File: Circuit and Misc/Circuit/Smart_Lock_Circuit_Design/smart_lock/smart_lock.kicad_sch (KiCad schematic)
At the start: 28 parts, among them J1 OLED, J2 RTC, J3 4x4 Keypad, J4 Ultrasonic sensor, J5 GSM, J6 Fingerprint sensor, J7 Bluetooth, Q1 IRLZ44N, Q2 BC547, SW1 Indoor button, SW2 Outdoor button, U1 24LC16, U2 LM358, U3 LM2596, U4 LM2596, U5 LM2596, U6 Bluepill_LDO, U7 STM32F103C8Tx

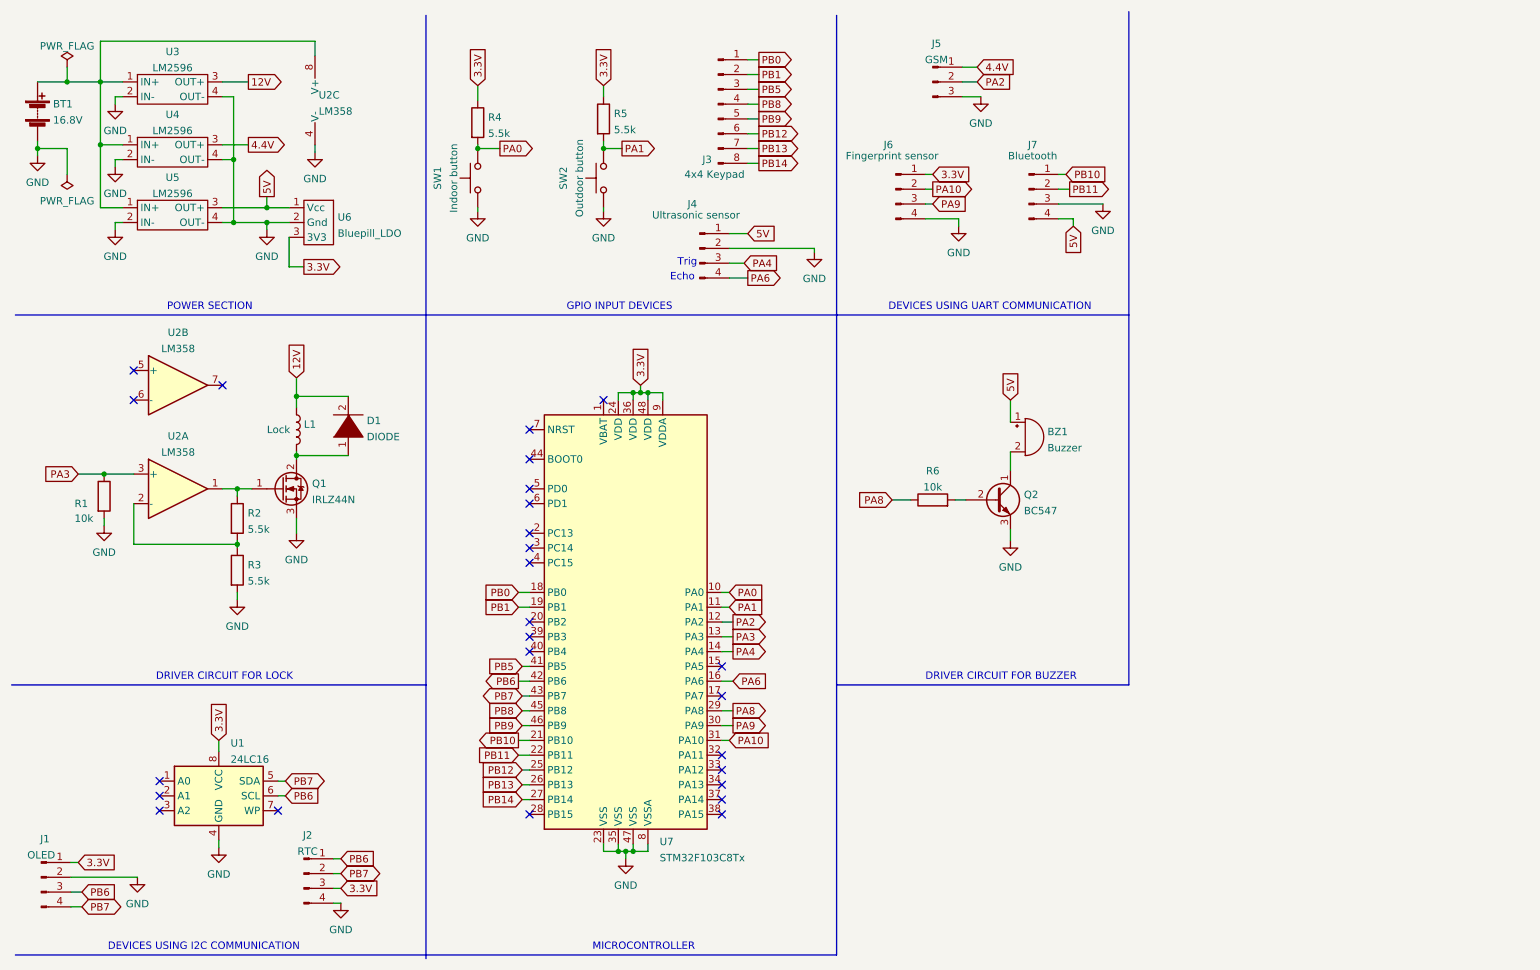
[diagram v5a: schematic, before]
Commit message: update
- Adjusted schematic (DY50 sensor is now powered using 5V)
- Added new images
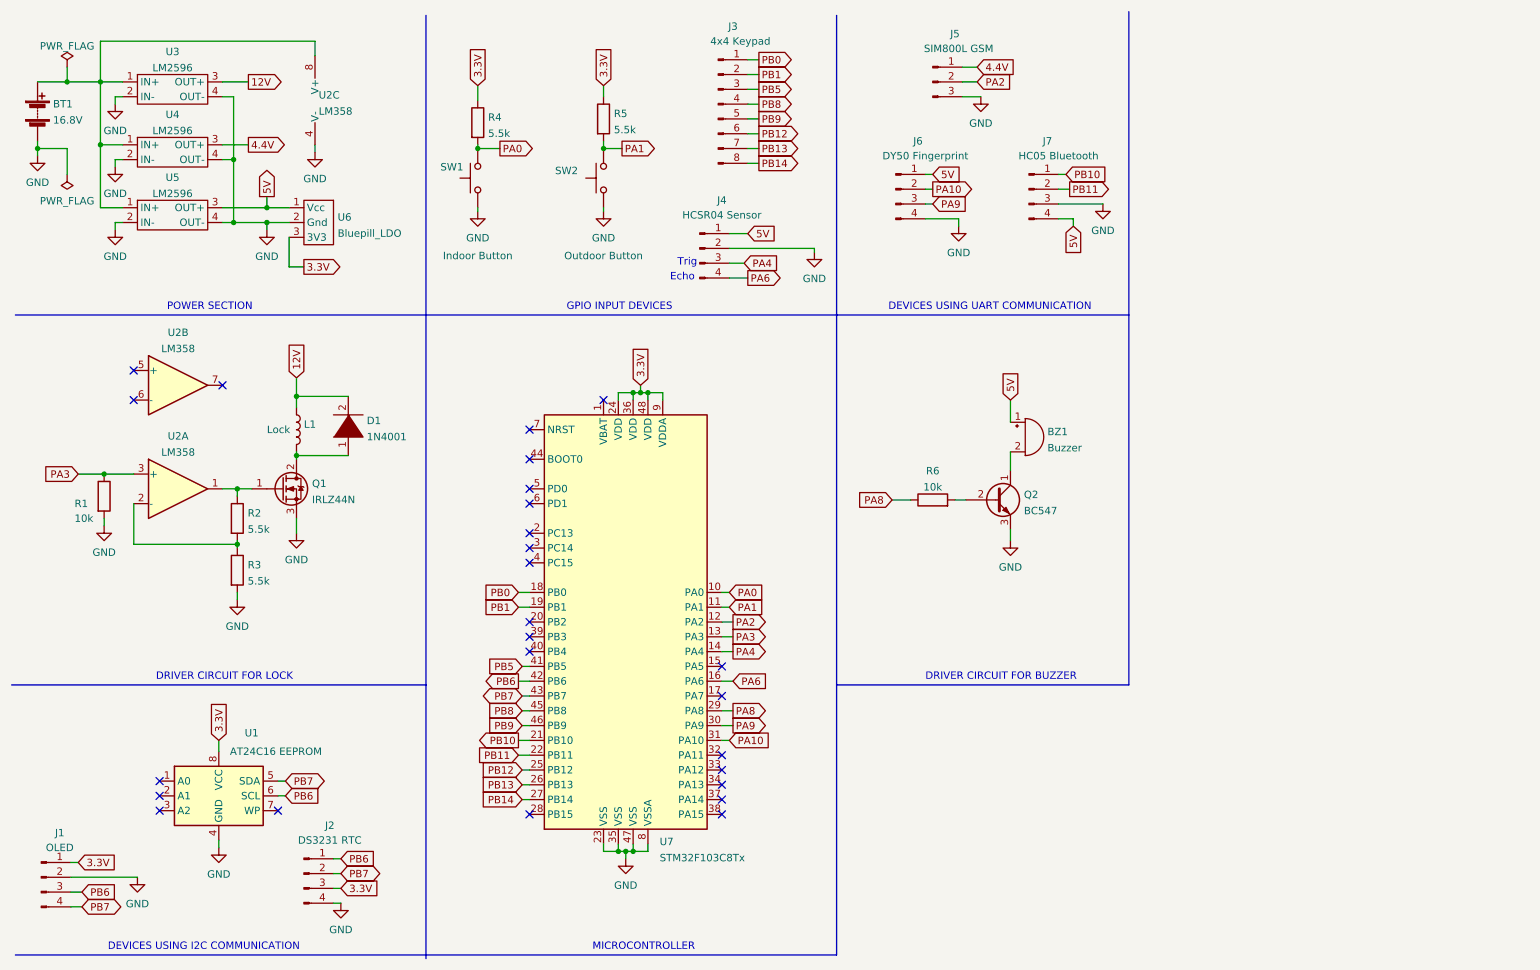
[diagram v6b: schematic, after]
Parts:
- D1: value DIODE -> 1N4001
- J2: value RTC -> DS3231 RTC
- J4: value Ultrasonic sensor -> HCSR04 Sensor
- J5: value GSM -> SIM800L GSM
- J6: value Fingerprint sensor -> DY50 Fingerprint
- J7: value Bluetooth -> HC05 Bluetooth
- SW1: value Indoor button -> Indoor Button
- SW2: value Outdoor button -> Outdoor Button
- U1: value 24LC16 -> AT24C16 EEPROM
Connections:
- net 3.3V: no longer J6.1 (Pin_1)
- net 5V: now also J6.1 (Pin_1)
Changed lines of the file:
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@@
     )
   )
-  (global_label "3.3V" (shape input) (at 169.545 39.37 0) (fields_autoplaced)
-    (effects (font (size 1.27 1.27)) (justify left))
-    (property "Intersheet References" "${INTERSHEET_REFS}" (id 0) (at 176.0705 39.2906 0)
+  (global_label "5V" (shape input) (at 169.545 39.37 0) (fields_autoplaced)
+    (effects (font (size 1.27 1.27)) (justify left))
+    (property "Intersheet References" "${INTERSHEET_REFS}" (id 0) (at 174.2562 39.2906 0)
       (effects (font (size 1.27 1.27)) (justify left) hide)
     )
@@
   )
   (symbol (lib_id "Switch:SW_MEC_5G") (at 91.44 40.005 90) (unit 1)
-    (in_bom yes) (on_board yes) (fields_autoplaced)
-    (property "Reference" "SW1" (id 0) (at 84.5525 40.005 0))
-    (property "Value" "Indoor button" (id 1) (at 87.3276 40.005 0))
+    (in_bom yes) (on_board yes)
+    (property "Reference" "SW1" (id 0) (at 86.995 38.1 90))
+    (property "Value" "Indoor Button" (id 1) (at 91.44 53.34 90))
     (property "Footprint" "" (id 2) (at 86.36 40.005 0)
       (effects (font (size 1.27 1.27)) hide)
@@
   )
   (symbol (lib_id "Connector:Conn_01x04_Male") (at 61.595 159.385 0) (unit 1)
-    (in_bom yes) (on_board yes) (fields_autoplaced)
-    (property "Reference" "J2" (id 0) (at 62.23 152.8023 0))
-    (property "Value" "RTC" (id 1) (at 62.23 155.5774 0))
+    (in_bom yes) (on_board yes)
+    (property "Reference" "J2" (id 0) (at 66.04 151.13 0))
+    (property "Value" "DS3231 RTC" (id 1) (at 66.04 153.67 0))
     (property "Footprint" "" (id 2) (at 61.595 159.385 0)
       (effects (font (size 1.27 1.27)) hide)
@@
   (symbol (lib_id "Connector:Conn_01x08_Male") (at 132.715 27.305 0) (unit 1)
     (in_bom yes) (on_board yes)
-    (property "Reference" "J3" (id 0) (at 130.81 36.83 0))
-    (property "Value" "4x4 Keypad" (id 1) (at 132.08 39.37 0))
+    (property "Reference" "J3" (id 0) (at 135.255 13.97 0))
+    (property "Value" "4x4 Keypad" (id 1) (at 136.525 16.51 0))
     (property "Footprint" "" (id 2) (at 132.715 27.305 0)
       (effects (font (size 1.27 1.27)) hide)
@@
       (effects (font (size 1.27 1.27)) (justify right))
     )
-    (property "Value" "DIODE" (id 1) (at 72.39 84.4166 90)
+    (property "Value" "1N4001" (id 1) (at 72.39 84.4166 90)
       (effects (font (size 1.27 1.27)) (justify right))
     )
@@
   (symbol (lib_id "Connector:Conn_01x04_Male") (at 163.195 41.91 0) (unit 1)
     (in_bom yes) (on_board yes)
-    (property "Reference" "J6" (id 0) (at 161.925 34.29 0))
-    (property "Value" "Fingerprint sensor" (id 1) (at 162.56 36.195 0))
+    (property "Reference" "J6" (id 0) (at 167.005 33.655 0))
+    (property "Value" "DY50 Fingerprint" (id 1) (at 168.275 36.195 0))
     (property "Footprint" "" (id 2) (at 163.195 41.91 0)
       (effects (font (size 1.27 1.27)) hide)
@@
   (symbol (lib_id "Connector:Conn_01x04_Male") (at 186.055 41.91 0) (unit 1)
     (in_bom yes) (on_board yes)
-    (property "Reference" "J7" (id 0) (at 186.69 34.29 0))
-    (property "Value" "Bluetooth" (id 1) (at 186.69 36.195 0))
+    (property "Reference" "J7" (id 0) (at 189.23 33.655 0))
+    (property "Value" "HC05 Bluetooth" (id 1) (at 191.135 36.195 0))
     (property "Footprint" "" (id 2) (at 186.055 41.91 0)
       (effects (font (size 1.27 1.27)) hide)
@@
   (symbol (lib_id "Connector:Conn_01x04_Male") (at 16.51 160.02 0) (unit 1)
     (in_bom yes) (on_board yes)
-    (property "Reference" "J1" (id 0) (at 17.145 153.4373 0))
-    (property "Value" "OLED" (id 1) (at 16.51 156.21 0))
+    (property "Reference" "J1" (id 0) (at 19.685 152.4 0))
+    (property "Value" "OLED" (id 1) (at 19.685 154.94 0))
     (property "Footprint" "" (id 2) (at 16.51 160.02 0)
       (effects (font (size 1.27 1.27)) hide)
@@
   )
   (symbol (lib_id "Switch:SW_MEC_5G") (at 113.03 40.005 90) (unit 1)
-    (in_bom yes) (on_board yes) (fields_autoplaced)
-    (property "Reference" "SW2" (id 0) (at 106.1425 40.005 0))
-    (property "Value" "Outdoor button" (id 1) (at 108.9176 40.005 0))
+    (in_bom yes) (on_board yes)
+    (property "Reference" "SW2" (id 0) (at 106.68 38.735 90))
+    (property "Value" "Outdoor Button" (id 1) (at 113.03 53.34 90))
     (property "Footprint" "" (id 2) (at 107.95 40.005 0)
       (effects (font (size 1.27 1.27)) hide)
@@
   )
   (symbol (lib_id "Connector:Conn_01x03_Male") (at 169.545 23.495 0) (unit 1)
-    (in_bom yes) (on_board yes) (fields_autoplaced)
-    (property "Reference" "J5" (id 0) (at 170.18 16.9123 0))
-    (property "Value" "GSM" (id 1) (at 170.18 19.6874 0))
+    (in_bom yes) (on_board yes)
+    (property "Reference" "J5" (id 0) (at 173.355 15.24 0))
+    (property "Value" "SIM800L GSM" (id 1) (at 173.99 17.78 0))
     (property "Footprint" "" (id 2) (at 169.545 23.495 0)
       (effects (font (size 1.27 1.27)) hide)
@@
   (symbol (lib_id "Connector:Conn_01x04_Male") (at 129.54 52.07 0) (unit 1)
     (in_bom yes) (on_board yes)
-    (property "Reference" "J4" (id 0) (at 128.27 44.45 0))
-    (property "Value" "Ultrasonic sensor" (id 1) (at 128.905 46.355 0))
+    (property "Reference" "J4" (id 0) (at 133.35 43.815 0))
+    (property "Value" "HCSR04 Sensor" (id 1) (at 133.35 46.355 0))
     (property "Footprint" "" (id 2) (at 129.54 52.07 0)
       (effects (font (size 1.27 1.27)) hide)
@@
   )
   (symbol (lib_id "Memory_EEPROM:24LC16") (at 46.99 146.05 0) (unit 1)
-    (in_bom yes) (on_board yes) (fields_autoplaced)
-    (property "Reference" "U1" (id 0) (at 49.0094 137.0035 0)
-      (effects (font (size 1.27 1.27)) (justify left))
-    )
-    (property "Value" "24LC16" (id 1) (at 49.0094 139.7786 0)
+    (in_bom yes) (on_board yes)
+    (property "Reference" "U1" (id 0) (at 51.435 135.255 0)
+      (effects (font (size 1.27 1.27)) (justify left))
+    )
+    (property "Value" "AT24C16 EEPROM" (id 1) (at 48.895 138.43 0)
       (effects (font (size 1.27 1.27)) (justify left))
     )
@@
     )
     (path "/4056a76c-ed40-4375-8958-fab8c8eb89d1"
-      (reference "D1") (unit 1) (value "DIODE") (footprint "")
+      (reference "D1") (unit 1) (value "1N4001") (footprint "")
     )
     (path "/afd6fb87-d45c-4852-9f08-1c8c55a437eb"
@@
     )
     (path "/20c33140-ecd1-4692-9348-d283c442c84a"
-      (reference "J2") (unit 1) (value "RTC") (footprint "")
+      (reference "J2") (unit 1) (value "DS3231 RTC") (footprint "")
     )
     (path "/2f1749e1-abed-43a9-8bd4-d14296cc65d4"
@@
     )
     (path "/bc6effc8-87db-4893-b9a4-0083d7cf18d2"
-      (reference "J4") (unit 1) (value "Ultrasonic sensor") (footprint "")
+      (reference "J4") (unit 1) (value "HCSR04 Sensor") (footprint "")
     )
     (path "/ba332a8c-8cb0-4198-9add-89840c85b387"
-      (reference "J5") (unit 1) (value "GSM") (footprint "")
+      (reference "J5") (unit 1) (value "SIM800L GSM") (footprint "")
     )
     (path "/646e5826-cfc5-4ede-99de-2709b41ef9ce"
-      (reference "J6") (unit 1) (value "Fingerprint sensor") (footprint "")
+      (reference "J6") (unit 1) (value "DY50 Fingerprint") (footprint "")
     )
     (path "/74064faa-1231-4f94-8bcd-c04841594ac4"
-      (reference "J7") (unit 1) (value "Bluetooth") (footprint "")
+      (reference "J7") (unit 1) (value "HC05 Bluetooth") (footprint "")
     )
     (path "/0b92809b-d176-4af4-a2a4-e98b7f81352e"
@@
     )
     (path "/0bb1e98a-12cb-4b3f-938c-9cfda3256758"
-      (reference "SW1") (unit 1) (value "Indoor button") (footprint "")
+      (reference "SW1") (unit 1) (value "Indoor Button") (footprint "")
     )
     (path "/b9349937-f4be-4789-b58b-595f2ab9279b"
-      (reference "SW2") (unit 1) (value "Outdoor button") (footprint "")
+      (reference "SW2") (unit 1) (value "Outdoor Button") (footprint "")
     )
     (path "/da65d86f-f94d-4db5-8413-9b29c5e2c0d0"
-      (reference "U1") (unit 1) (value "24LC16") (footprint "")
+      (reference "U1") (unit 1) (value "AT24C16 EEPROM") (footprint "")
     )
     (path "/3a1142ec-0e07-4e47-a6a1-757767a49405"
